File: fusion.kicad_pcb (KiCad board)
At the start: 2 copper layers, 276.2 x 92.3 mm, 95 parts, among them J1 Conn_01x04_Female, J2 USB_C_Receptacle_USB2.0, J3 Conn_01x12_MountingPin, J4 Conn_01x12_MountingPin, J5 Conn_02x10_Odd_Even_MountingP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, K1 diode-choc, K10 diode-choc, K11 diode-choc, K12 diode-choc, K13 diode-choc, K14 diode-choc, K15 diode-choc, K16 diode-choc, K17 diode-choc, K18 diode-choc, K19 diode-choc, K2 diode-choc, K20 diode-choc, K21 diode-choc, K22 diode-choc, K23 diode-choc, K24 diode-choc, K25 diode-choc, K26 diode-choc, K27 diode-choc, K28 diode-choc, K29 diode-choc, K3 diode-choc, K30 diode-choc, K31 diode-choc, K32 diode-choc, K33 diode-choc, K34 diode-choc, K35 diode-choc, K36 diode-choc, K37 diode-choc, K38 diode-choc, K4 diode-choc, K5 diode-choc, K6 diode-choc, K7 diode-choc, K8 diode-choc, K9 diode-choc, SW1 SW_Push, SW2 SW_SPDT, U1 Holyiot_18010_no_underside, U2 MT25QL128ABA1ESE, U3 BQ24075, U4 XC6220B331MR, U5 LN4913, U6 MIC5365-2.8YC5, U7 4050, U8 SRV05-4

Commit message: update PCB
use cirque trackpad, increase angle to 22.5
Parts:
- removed C6: 0.1uF, Capacitor_SMD:C_0603_1608Metric
- removed H1: touchpad, fusion:touchpad-holder
- removed H15: sensor-magnet, fusion:sensor-magnet
- removed the H2 at (159.0, 48.2)
- removed the H2 at (39.5, 48.2)
- removed the H4 at (127.8, 54.2)
- removed the H4 at (70.7, 54.2)
- removed JP1, JP2, JP3: SolderJumper_2_Open, Jumper:SolderJumper-2_P1.3mm_Open_RoundedPad1.0x1.5mm
- removed R11, R4: 220k, Resistor_SMD:R_0603_1608Metric
- removed U6: MIC5365-2.8YC5, Package_TO_SOT_SMD:SOT-23-5
- removed U7: 4050, Package_SO:SOIC-16_3.9x9.9mm_P1.27mm
- added H2: mouse-bite, Keebio-Parts:breakaway-mousebites, F.Cu at (209.5, 51.2)
- added H2: mouse-bite, Keebio-Parts:breakaway-mousebites, B.Cu at (93.1, 51.2)
- added H4: mouse-bite, Keebio-Parts:breakaway-mousebites, F.Cu at (181.9, 62.6)
- added H4: mouse-bite, Keebio-Parts:breakaway-mousebites, B.Cu at (120.6, 62.6)
- added JP4: SolderJumper_2_Open, Jumper:SolderJumper-2_P1.3mm_Open_RoundedPad1.0x1.5mm, F.Cu at (164.0, 94.4)
- added REF**: touchpad-holder, fusion:touchpad-holder, F.Cu at (241.6, 98.9)
- added REF**: MountingHole_2.2mm_M2, MountingHole:MountingHole_2.2mm_M2, F.Cu at (134.0, 79.6)
- H20: footprint fusion:bat-shell -> fusion:bat-shell-small
- J1: value Conn_01x04_Female -> debug-port; footprint keeb-libs:debug-port-single-side -> misc:debug-port-single-side
- J5: value Conn_02x10_Odd_Even_MountingPin -> cirque-trackpad; footprint keeb-libs:hirose-df30fb-20ds-0.4v(82) -> Connector_FFC-FPC:Hirose_FH12-12S-0.5SH_1x12-1MP_P0.50mm_Horizontal
- LCD1: value SHARP_LCD -> adafruit-sharp-memory-display-no-useless; footprint keeb-libs:Adafruit-Sharp-Memory-Display-1.3in-no-mounting -> display:adafruit-sharp-memory-display-1.3in-no-mounting-no-useless
- U1: value Holyiot_18010_no_underside -> holyiot-18010-no-underside; footprint keeb-libs:Holyiot-18010-no-underside -> mcu:holyiot-18010-no-underside
- U2: footprint Package_SO:SOP-8_5.28x5.23mm_P1.27mm -> Package_SO:SOIC-8_5.23x5.23mm_P1.27mm
- U4: value XC6220B331MR -> XC6206B331MR
- moved SW1 70.2 mm to (196.0, 108.9), turned to 180 degrees
- moved H20 67.1 mm to (115.5, 138.6), turned to 15 degrees
- moved K38 59.8 mm to (208.0, 127.9), turned to -67.5 degrees
- moved K37 58.9 mm to (219.5, 120.5), turned to -67.5 degrees
- moved K36 58.1 mm to (231.4, 113.9), turned to -67.5 degrees
- moved R14 56.2 mm to (183.4, 108.3)
- moved R13 56.2 mm to (184.9, 108.3)
- moved R12 56.2 mm to (186.4, 108.3)
- moved H18 55.5 mm to (258.8, 87.9)
- moved K29 55.4 mm to (272.0, 87.5), turned to 22.5 degrees
- moved K33 55.2 mm to (203.9, 93.0), turned to 22.5 degrees
- moved J3 55.1 mm to (131.8, 96.4)
- moved J4 54.7 mm to (170.8, 96.4)
- moved LCD1 54.6 mm to (177.0, 115.2)
- moved U1 54.6 mm to (167.5, 110.5)
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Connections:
- net VDDH renamed /power/VDDH
- D2 pad 2: VDD -> +3V3
- J1 pad 2: VDD -> +3V3
- J1 pad 3: SWC -> SWD
- J1 pad 4: SWD -> SWC
- J5 pad 1: GND -> +3V3
- J5 pad 10: Net-(J5-Pad10) -> TP_~{CS}
- J5 pad 11: SCK_2V8 -> MISO_DQ1
- J5 pad 12: +2V8 -> SCLK
- J5 pad 2: unconnected-(J5-Pad2) -> GND
- J5 pad 5: GND -> TP_BTN1
- J5 pad 6: unconnected-(J5-Pad6) -> TP_BTN3
- J5 pad 7: SHTDWN_2V8 -> TP_BTN2
- J5 pad 8: unconnected-(J5-Pad8) -> MOSI_DQ0
- J5 pad 9: ~{CS}_2V8 -> TP_DR
- J5 pad MP: GND -> (no net)
- LCD1 pad 1: unconnected-(LCD1-Pad1) -> DISP_~{CS}
- LCD1 pad 2: unconnected-(LCD1-Pad2) -> MOSI_DQ0
- LCD1 pad 3: unconnected-(LCD1-Pad3) -> SCLK
- LCD1 pad 4: DISP_~{CS} -> GND
- LCD1 pad 5: MOSI_DQ0 -> +3V3
- R3 pad 1: VDD -> +3V3
- U1 pad 10: TRACKPAD_~{CS} -> TP_~{CS}
- U1 pad 33: C4 -> Net-(JP4-Pad1)
- U1 pad 34: R0 -> C4
- U1 pad 35: R1 -> R0
- U1 pad 36: R2 -> R1
- U1 pad 39: R3 -> R2
- U1 pad 40: MAGNET -> R3
- U1 pad 43: TOUCHPAD_BTN -> TP_DR
- U1 pad 5: C3 -> R7
- U1 pad 52: R6 -> FLASH_~{CS}
- U1 pad 53: FLASH_~{CS} -> R6
- U1 pad 55: VDD -> +3V3
- U1 pad 6: R7 -> C3
- U1 pad 8: MOTION -> unconnected-(U1-Pad8)
- U1 pad 9: SHTDWN -> unconnected-(U1-Pad9)
- U2 pad 8: VDD -> +3V3
- U4 pad 5: VDD -> +3V3
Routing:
- net VDD: track 139.4 -> 0.00 mm, vias 6 -> 0
- net +3V3: track 0.00 -> 114.3 mm, vias 0 -> 5
- net TOUCHPAD_BTN: track 80.6 -> 0.00 mm, vias 2 -> 0
- net MOTION: track 72.4 -> 0.00 mm, vias 2 -> 0
- net /trackpad-8520/MISO_2V8: track 69.9 -> 0.00 mm, vias 2 -> 0
- net /trackpad-8520/MOSI_3V3: track 66.6 -> 0.00 mm, vias 2 -> 0
- net SHTDWN: track 64.8 -> 0.00 mm, vias 2 -> 0
- net TRACKPAD_~{CS}: track 61.9 -> 0.00 mm, vias 2 -> 0
- net /trackpad-8520/SCK_3V3: track 55.9 -> 0.00 mm, vias 2 -> 0
- net /power/VDDH: track 100.2 -> 52.2 mm, vias 2 -> 0
- net TP_DR: track 0.00 -> 43.4 mm, vias 0 -> 2
- net TP_~{CS}: track 0.00 -> 40.9 mm, vias 0 -> 2
- net MAGNET: track 104.6 -> 65.5 mm, vias 3 -> 4
- net MOSI_DQ0: track 19.1 -> 51.7 mm, vias 0 -> 2
- net MISO_DQ1: track 14.8 -> 44.2 mm, vias 0 -> 2
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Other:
- board size 276.2 x 92.3 mm -> 280 x 97.1 mm
- board text removed: "MISO"
- board text removed: "MOSI"
- board text removed: "SCLK"
- board text removed: "rough shadow of a 45 deg trackpad"

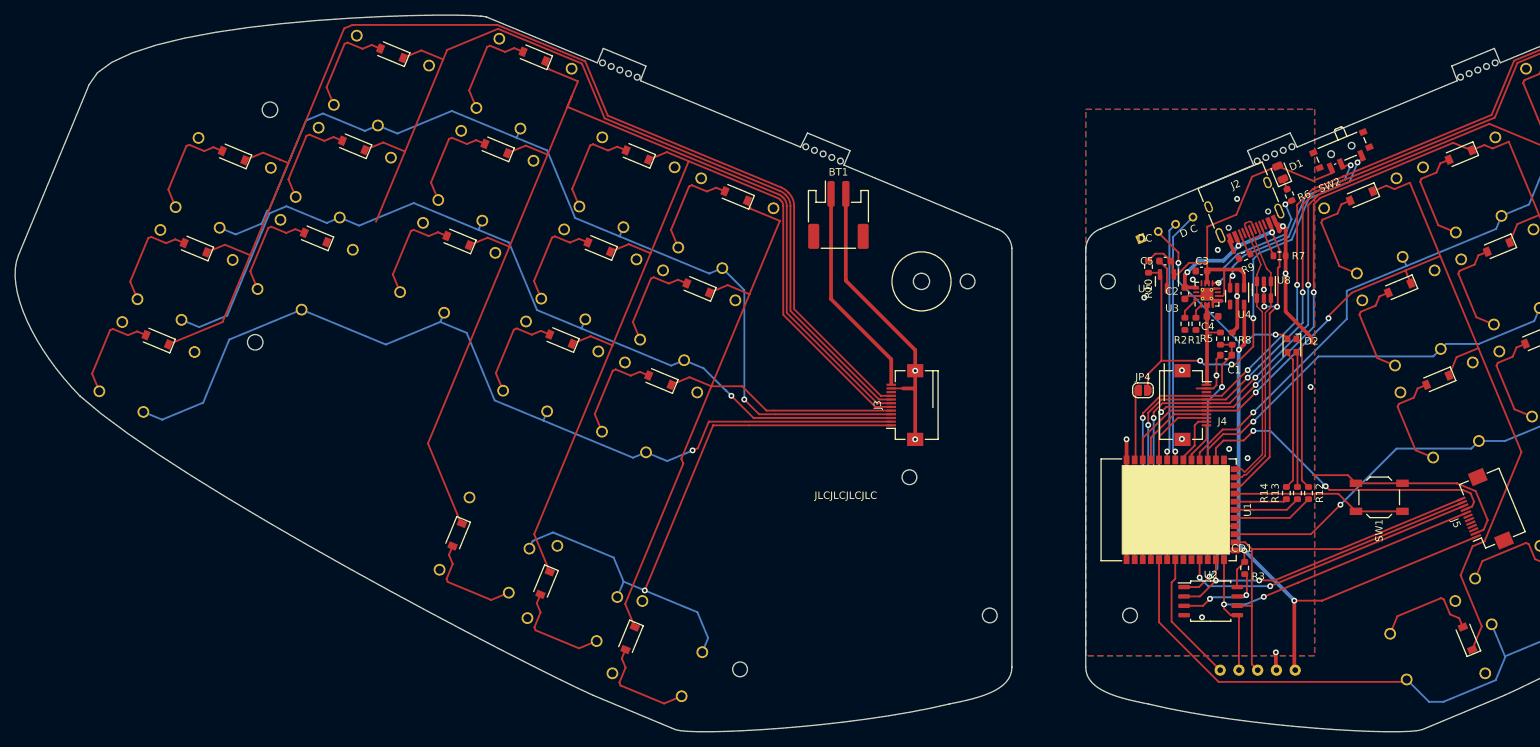
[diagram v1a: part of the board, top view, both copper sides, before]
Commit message: add assembly tooling hole
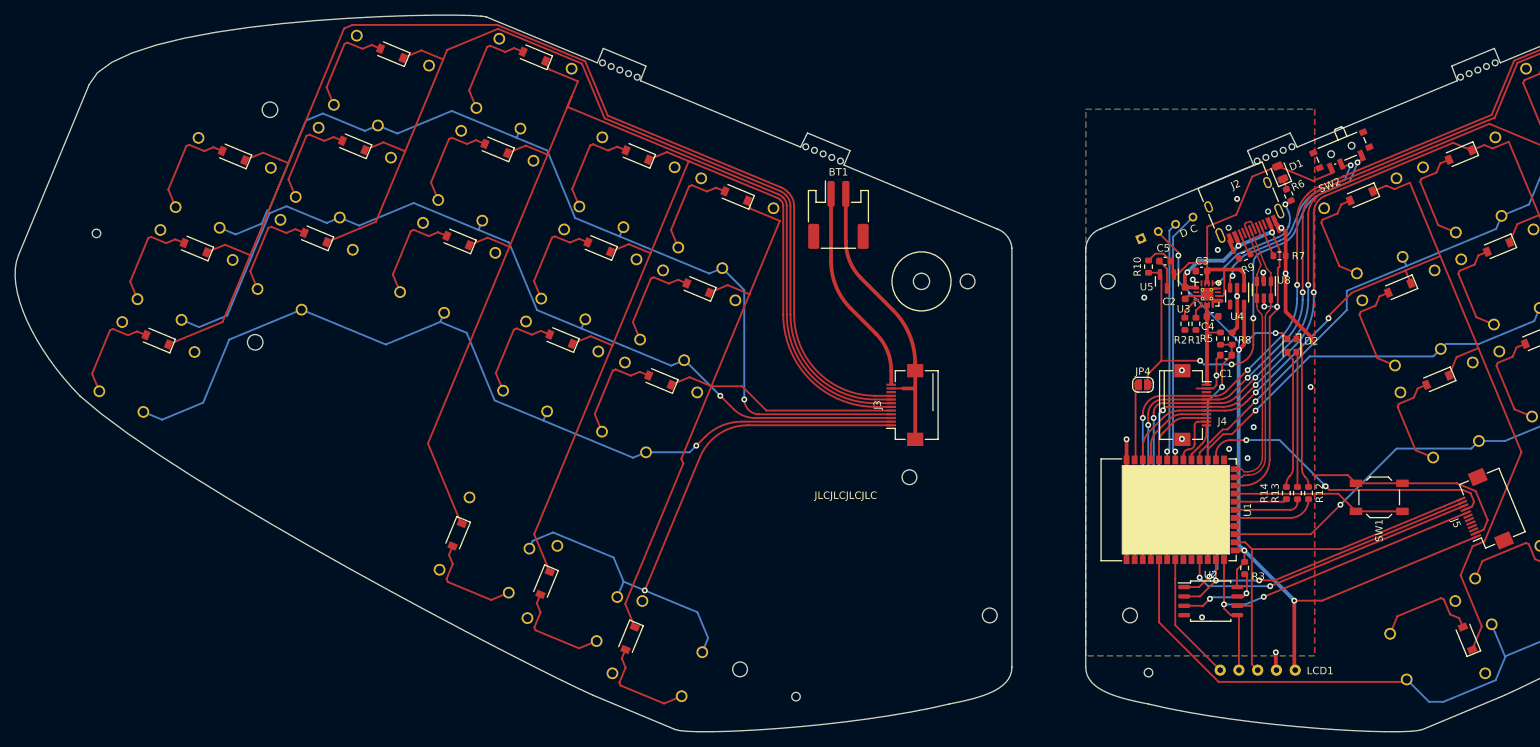
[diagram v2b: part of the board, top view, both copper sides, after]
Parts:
- added REF**: jlc-tooling-hole, misc:jlc-tooling-hole, F.Cu at (117.0, 135.9)
- added REF**: jlc-tooling-hole, misc:jlc-tooling-hole, F.Cu at (22.3, 73.1)
- added REF**: jlc-tooling-hole, misc:jlc-tooling-hole, F.Cu at (164.8, 132.6)
- moved JP4 0.75 mm to (164.0, 93.6)
- moved R6 0.10 mm to (183.8, 67.9)
- moved C2 0.05 mm to (169.7, 81.2)
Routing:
- net /left/C1: track 125.9 -> 134.8 mm
- net /left/R2: track 123.8 -> 122.2 mm
- net /left/C0: track 166.3 -> 167.9 mm
- net /left/C3: track 126.8 -> 128.3 mm
- net /left/C2: track 150.3 -> 151.7 mm
- net TP_DR: track 43.4 -> 42.1 mm
- net /left/R3: track 83.8 -> 82.6 mm
- net MAGNET: track 65.5 -> 64.4 mm
- net /left/GND: track 40.3 -> 39.5 mm, vias 2 -> 0
- net /left/BAT: track 29.1 -> 28.4 mm
- net C3: track 169.6 -> 168.9 mm
- net R4: track 133.1 -> 132.4 mm
- net MISO_DQ1: track 44.2 -> 43.5 mm
- net C2: track 204.3 -> 203.7 mm
- net C1: track 191.0 -> 190.4 mm
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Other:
- board text removed: "DC"

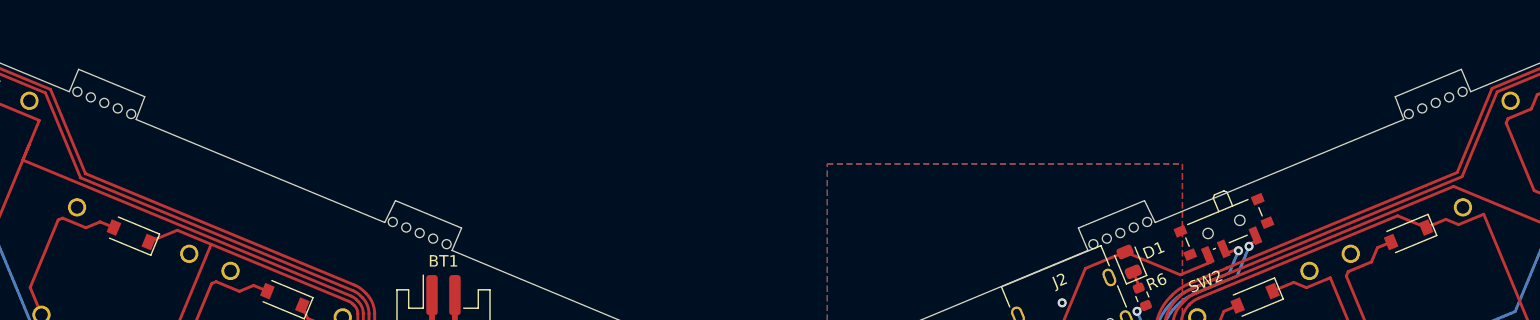
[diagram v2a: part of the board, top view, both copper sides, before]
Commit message: shell & adhesive cutting lines for the back
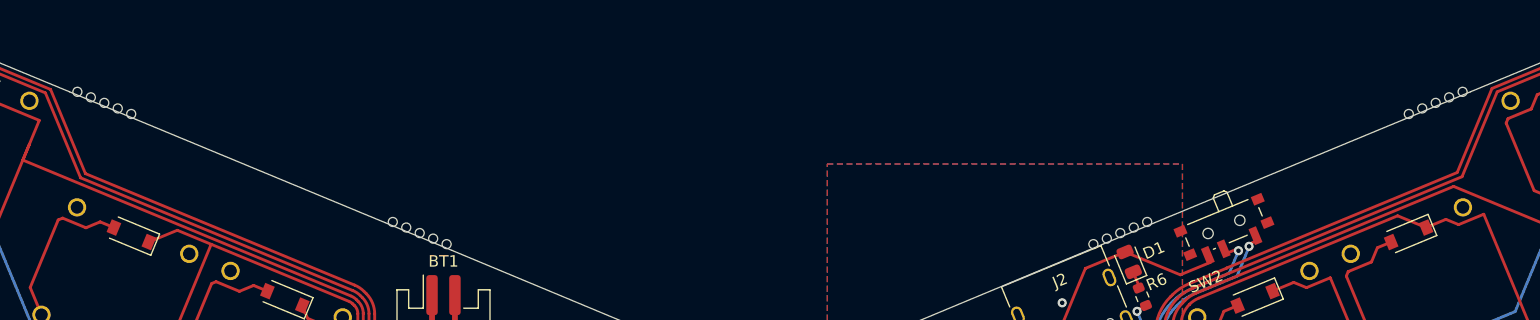
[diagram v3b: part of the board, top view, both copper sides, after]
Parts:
- added REF**: pg1232-cut, pg1232:pg1232-cut, F.Cu at (90.4, 75.0)
- added REF**: pg1232-cut, pg1232:pg1232-cut, F.Cu at (57.1, 61.2)
- added REF**: pg1232-cut, pg1232:pg1232-cut, F.Cu at (103.7, 80.5)
- added REF**: pg1232-cut, pg1232:pg1232-cut, F.Cu at (40.8, 62.6)
- added REF**: pg1232-cut, pg1232:pg1232-cut, F.Cu at (95.5, 62.5)
- added REF**: pg1232-cut, pg1232:pg1232-cut, F.Cu at (231.3, 74.1)
- added REF**: pg1232-cut, pg1232:pg1232-cut, F.Cu at (203.9, 93.0)
- added REF**: pg1232-cut, pg1232:pg1232-cut, F.Cu at (275.1, 57.0)
- added REF**: pg1232-cut, pg1232:pg1232-cut, F.Cu at (266.9, 75.0)
- added REF**: pg1232-cut, pg1232:pg1232-cut, F.Cu at (81.6, 49.1)
- added REF**: pg1232-cut, pg1232:pg1232-cut, F.Cu at (212.2, 75.0)
- added REF**: pg1232-cut, pg1232:pg1232-cut, F.Cu at (193.6, 68.0)
- added REF**: pg1232-cut, pg1232:pg1232-cut, F.Cu at (51.9, 73.7)
- added REF**: pg1232-cut, pg1232:pg1232-cut, F.Cu at (250.6, 73.7)
- added REF**: pg1232-cut, pg1232:pg1232-cut, F.Cu at (198.8, 80.5)
- added REF**: pg1232-cut, pg1232:pg1232-cut, F.Cu at (62.3, 48.7)
- added REF**: pg1232-cut, pg1232:pg1232-cut, F.Cu at (226.1, 61.6)
- added REF**: pg1232-cut, pg1232:pg1232-cut, F.Cu at (98.6, 93.0)
- added REF**: pg1232-cut, pg1232:pg1232-cut, F.Cu at (85.2, 87.4)
- added REF**: pg1232-cut, pg1232:pg1232-cut, F.Cu at (94.5, 127.9)
- added REF**: pg1232-cut, pg1232:pg1232-cut, F.Cu at (221.0, 49.1)
- added REF**: pg1232-cut, pg1232:pg1232-cut, F.Cu at (231.4, 113.9)
- added REF**: pg1232-cut, pg1232:pg1232-cut, F.Cu at (240.3, 48.7)
- added REF**: pg1232-cut, pg1232:pg1232-cut, F.Cu at (71.1, 113.9)
- added REF**: pg1232-cut, pg1232:pg1232-cut, F.Cu at (30.5, 87.5)
- added REF**: pg1232-cut, pg1232:pg1232-cut, F.Cu at (76.4, 61.6)
- added REF**: pg1232-cut, pg1232:pg1232-cut, F.Cu at (272.0, 87.5)
- added REF**: pg1232-cut, pg1232:pg1232-cut, F.Cu at (71.2, 74.1)
- added REF**: pg1232-cut, pg1232:pg1232-cut, F.Cu at (35.7, 75.0)
- added REF**: pg1232-cut, pg1232:pg1232-cut, F.Cu at (261.7, 62.6)
- added REF**: pg1232-cut, pg1232:pg1232-cut, F.Cu at (208.0, 127.9)
- added REF**: pg1232-cut, pg1232:pg1232-cut, F.Cu at (207.0, 62.5)
- added REF**: pg1232-cut, pg1232:pg1232-cut, F.Cu at (217.3, 87.4)
- added REF**: pg1232-cut, pg1232:pg1232-cut, F.Cu at (219.5, 120.5)
- added REF**: pg1232-cut, pg1232:pg1232-cut, F.Cu at (245.4, 61.2)
- added REF**: pg1232-cut, pg1232:pg1232-cut, F.Cu at (83.0, 120.5)
- added REF**: pg1232-cut, pg1232:pg1232-cut, F.Cu at (280.3, 69.5)
- added REF**: pg1232-cut, pg1232:pg1232-cut, F.Cu at (108.9, 68.0)
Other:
- outline, holes or cut-outs redrawn

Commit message: new version
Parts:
- removed JP4: SolderJumper_2_Open, Jumper:SolderJumper-2_P1.3mm_Open_RoundedPad1.0x1.5mm
- removed the REF** at (90.4, 75.0)
- removed the REF** at (57.1, 61.2)
- removed the REF** at (103.7, 80.5)
- removed the REF** at (40.8, 62.6)
- removed the REF** at (95.5, 62.5)
- removed the REF** at (231.3, 74.1)
- removed the REF** at (203.9, 93.0)
- removed the REF** at (275.1, 57.0)
- removed the REF** at (266.9, 75.0)
- removed the REF** at (81.6, 49.1)
- removed the REF** at (212.2, 75.0)
- removed the REF** at (193.6, 68.0)
- removed the REF** at (51.9, 73.7)
- removed the REF** at (250.6, 73.7)
- removed the REF** at (198.8, 80.5)
- removed the REF** at (62.3, 48.7)
- removed the REF** at (226.1, 61.6)
- removed the REF** at (98.6, 93.0)
- removed the REF** at (85.2, 87.4)
- removed the REF** at (94.5, 127.9)
- removed the REF** at (221.0, 49.1)
- removed the REF** at (231.4, 113.9)
- removed the REF** at (240.3, 48.7)
- removed the REF** at (71.1, 113.9)
- removed the REF** at (30.5, 87.5)
- removed the REF** at (76.4, 61.6)
- removed the REF** at (272.0, 87.5)
- removed the REF** at (71.2, 74.1)
- removed the REF** at (35.7, 75.0)
- removed the REF** at (261.7, 62.6)
- removed the REF** at (208.0, 127.9)
- removed the REF** at (207.0, 62.5)
- removed the REF** at (217.3, 87.4)
- removed the REF** at (219.5, 120.5)
- removed the REF** at (245.4, 61.2)
- removed the REF** at (83.0, 120.5)
- removed the REF** at (280.3, 69.5)
- removed the REF** at (108.9, 68.0)
- added D3: D_Small, Diode_SMD:D_SOD-123, F.Cu at (164.2, 84.9)
- added REF**: pg1232-cut, pg1232:pg1232-cut, F.Cu at (225.5, 61.7)
- added REF**: pg1232-cut, pg1232:pg1232-cut, F.Cu at (75.8, 61.7)
- added REF** (x2): pg1232-cut, pg1232:pg1232-cut, F.Cu at (108.3, 68.2)
- added REF**: pg1232-cut, pg1232:pg1232-cut, F.Cu at (70.6, 74.2)
- added REF**: pg1232-cut, pg1232:pg1232-cut, F.Cu at (103.2, 80.7)
- added REF**: pg1232-cut, pg1232:pg1232-cut, F.Cu at (71.0, 113.5)
- added REF**: pg1232-cut, pg1232:pg1232-cut, F.Cu at (94.9, 62.6)
- added REF**: pg1232-cut, pg1232:pg1232-cut, F.Cu at (279.7, 69.6)
- added REF**: pg1232-cut, pg1232:pg1232-cut, F.Cu at (274.5, 57.2)
- added REF**: pg1232-cut, pg1232:pg1232-cut, F.Cu at (40.2, 62.7)
- added REF**: pg1232-cut, pg1232:pg1232-cut, F.Cu at (239.7, 48.9)
- added REF**: pg1232-cut, pg1232:pg1232-cut, F.Cu at (220.4, 49.3)
- added REF**: pg1232-cut, pg1232:pg1232-cut, F.Cu at (82.6, 120.5)
- added REF**: pg1232-cut, pg1232:pg1232-cut, F.Cu at (98.0, 93.1)
- added REF**: pg1232-cut, pg1232:pg1232-cut, F.Cu at (89.8, 75.1)
- added REF**: pg1232-cut, pg1232:pg1232-cut, F.Cu at (211.6, 75.1)
- added REF**: pg1232-cut, pg1232:pg1232-cut, F.Cu at (271.4, 87.7)
- added REF**: pg1232-cut, pg1232:pg1232-cut, F.Cu at (51.3, 73.8)
- added REF**: pg1232-cut, pg1232:pg1232-cut, F.Cu at (193.0, 68.2)
- added REF**: pg1232-cut, pg1232:pg1232-cut, F.Cu at (230.4, 113.6)
- added REF**: pg1232-cut, pg1232:pg1232-cut, F.Cu at (230.7, 74.2)
- added REF**: pg1232-cut, pg1232:pg1232-cut, F.Cu at (61.7, 48.9)
- added REF**: pg1232-cut, pg1232:pg1232-cut, F.Cu at (203.4, 93.1)
- added REF**: pg1232-cut, pg1232:pg1232-cut, F.Cu at (29.9, 87.7)
- added REF**: pg1232-cut, pg1232:pg1232-cut, F.Cu at (35.1, 75.2)
- added REF**: pg1232-cut, pg1232:pg1232-cut, F.Cu at (81.0, 49.3)
- added REF**: pg1232-cut, pg1232:pg1232-cut, F.Cu at (206.4, 62.6)
- added REF**: pg1232-cut, pg1232:pg1232-cut, F.Cu at (56.5, 61.3)
- added REF**: pg1232-cut, pg1232:pg1232-cut, F.Cu at (244.8, 61.3)
- added REF**: pg1232-cut, pg1232:pg1232-cut, F.Cu at (250.0, 73.8)
- added REF**: pg1232-cut, pg1232:pg1232-cut, F.Cu at (84.6, 87.6)
- added REF**: pg1232-cut, pg1232:pg1232-cut, F.Cu at (261.1, 62.7)
- added REF**: pg1232-cut, pg1232:pg1232-cut, F.Cu at (218.8, 120.5)
- added REF**: pg1232-cut, pg1232:pg1232-cut, F.Cu at (207.2, 127.4)
- added REF**: pg1232-cut, pg1232:pg1232-cut, F.Cu at (94.1, 127.4)
- added REF**: pg1232-cut, pg1232:pg1232-cut, F.Cu at (216.7, 87.6)
- added REF**: pg1232-cut, pg1232:pg1232-cut, F.Cu at (198.2, 80.7)
- added REF**: pg1232-cut, pg1232:pg1232-cut, F.Cu at (266.3, 75.2)
- J1: value debug-port -> tc2030; footprint misc:debug-port-single-side -> Connector:Tag-Connect_TC2030-IDC-NL_2x03_P1.27mm_Vertical
- moved H8 31.7 mm to (43.2, 88.0), turned to 22.5 degrees
- moved H9 31.4 mm to (45.2, 56.5), turned to 22.5 degrees
- moved REF** 26.8 mm to (138.0, 130.9), turned to -22.5 degrees
- moved J1 15.9 mm to (168.2, 88.2), turned to 0 degrees
- moved R2 2.15 mm to (168.4, 83.6), turned to 180 degrees
- moved C1 1.70 mm to (173.9, 90.6), turned to -90 degrees
- moved R1 1.30 mm to (169.9, 85.1), turned to 180 degrees
- moved SW1 1.15 mm to (196.9, 108.1)
- moved K36 1.06 mm to (230.4, 113.6), turned to -59.1 degrees
- moved K38 0.90 mm to (207.2, 127.4), turned to -59.1 degrees
- moved LCD1 0.81 mm to (177.7, 114.7)
- moved K37 0.68 mm to (218.8, 120.5), turned to -59.1 degrees
- moved K18 0.68 mm to (94.1, 127.4), turned to 59.1 degrees
- moved U1 0.60 mm to (166.9, 110.7)
- moved D1 0.60 mm to (182.0, 65.0)
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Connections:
- J1 pad 1: GND -> +3V3
- J1 pad 2: +3V3 -> SWD
- J1 pad 3: SWD -> RST
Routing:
- net RST: track 23.6 -> 51.1 mm, vias 0 -> 2
- net MAGNET: track 64.4 -> 47.7 mm, vias 4 -> 2
- net SWC: track 34.1 -> 19.2 mm, vias 1 -> 2
- net SWD: track 32.4 -> 19.0 mm, vias 1 -> 2
- net Net-(U1-Pad33): track 9.72 -> 19.1 mm
- net +3V3: track 114.1 -> 104.8 mm
- net GND: track 97.0 -> 103.4 mm, vias 21 -> 20
- net C2: track 203.7 -> 197.6 mm
- net C4: track 134.9 -> 133.1 mm
- net R7: track 195.5 -> 193.8 mm
- net /left/R3: track 82.6 -> 84.3 mm
- net /left/C2: track 151.7 -> 150.0 mm
- net BAT_MEAS: track 32.0 -> 33.2 mm
- net /left/C4: track 102.5 -> 101.3 mm
- net Net-(R2-Pad1): track 3.09 -> 2.00 mm
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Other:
- board size 280 x 97.1 mm -> 280 x 97 mm
